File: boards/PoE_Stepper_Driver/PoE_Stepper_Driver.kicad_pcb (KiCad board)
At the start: 2 copper layers, 76 parts, among them J1 RJ45, J2 Motor, Q1 NMOS_POE, Q10 NMOS_POE, Q3 NMOS_POE, Q4 NMOS_POE, Q5 NMOS_POE, Q6 NMOS_POE, Q7 NMOS_POE, Q8 NMOS_POE, Q9 NMOS_POE, SW3 SW_Push, U1 LT4321, U14 DP83848C, U15 TMC429-I, U16 TMC2660C-PA, U2 LT4293, U3 STM32F407VETx, U4 NCP1117, U5 E48SC12010, X1 SXO53C, Y1 8MHz

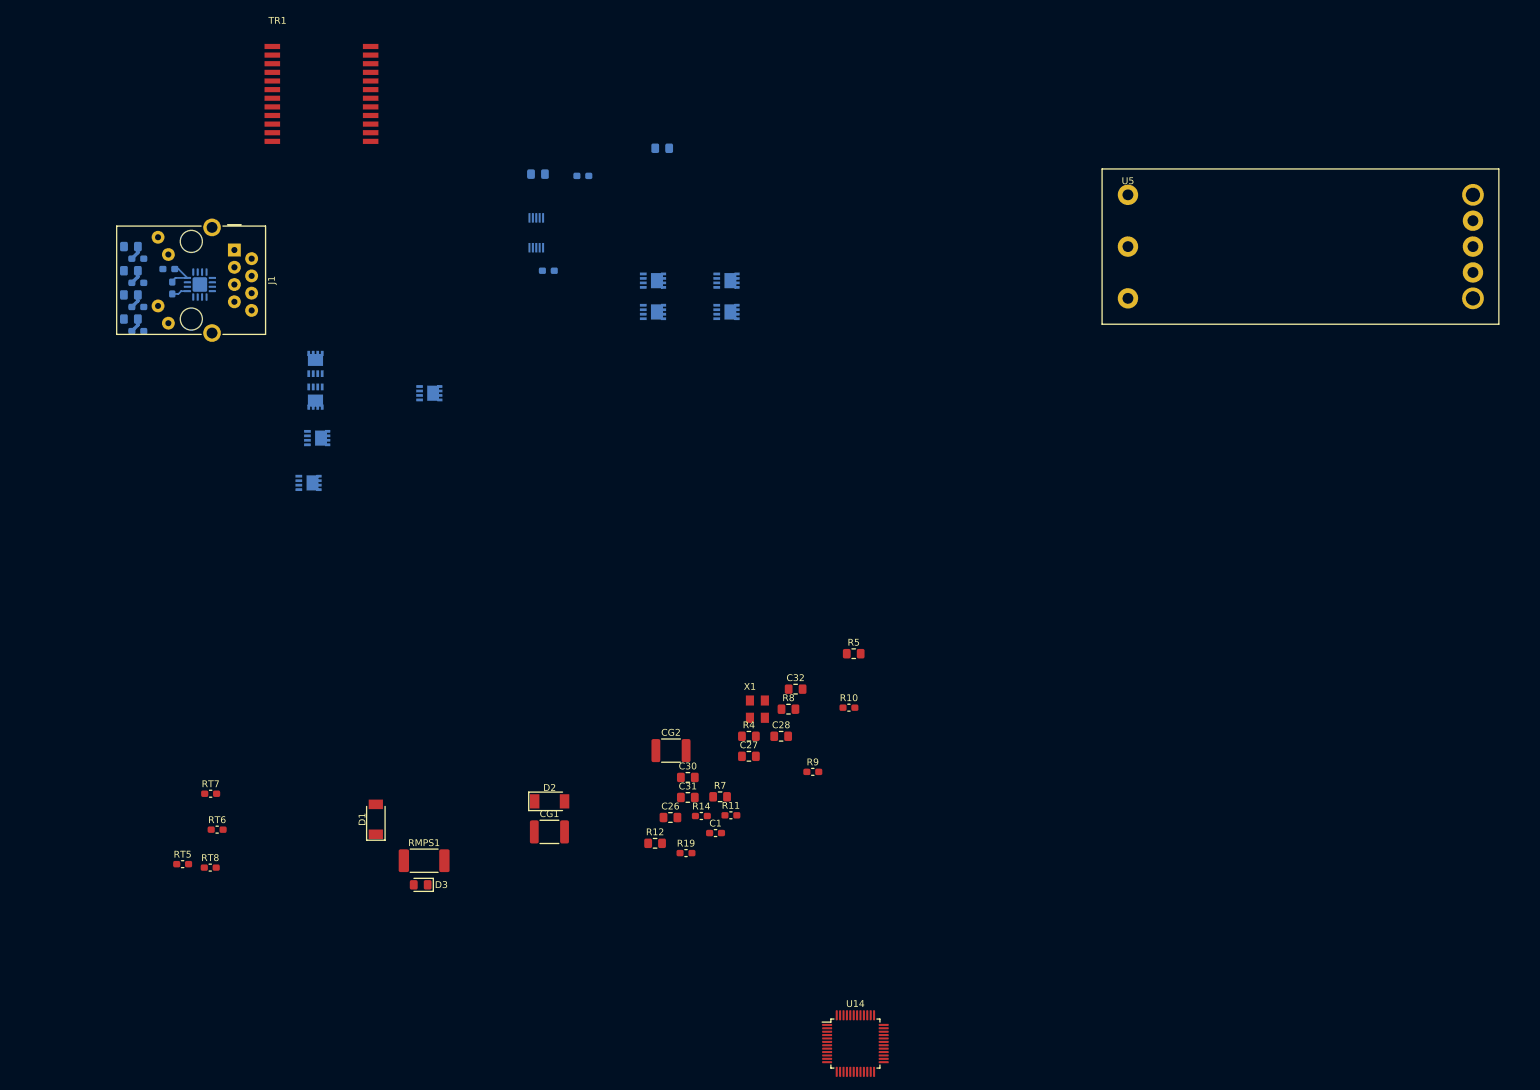
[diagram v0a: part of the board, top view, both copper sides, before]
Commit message: why tf is gnd connected to vout- bruhh
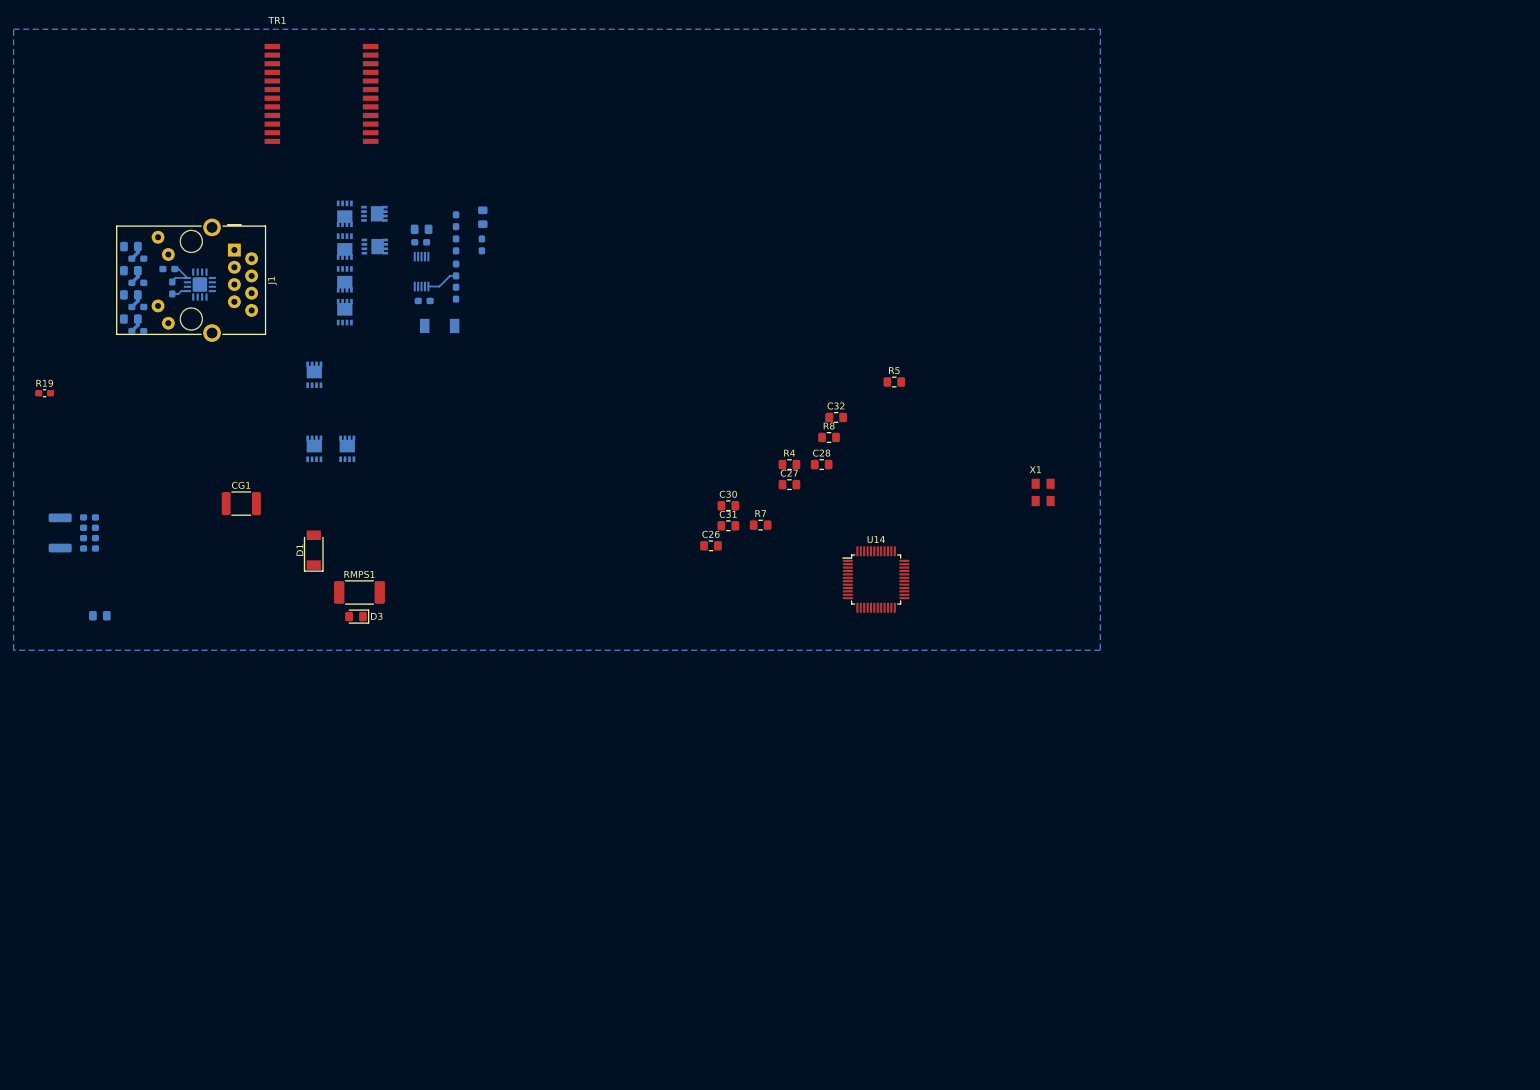
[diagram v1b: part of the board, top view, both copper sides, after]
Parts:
- removed U5: E48SC12010, PoE_Stepper_Driver:E48SC12010
- C1, CG2, D2, R10, R11, R12, R14, R9, RT5, RT6, RT7, RT8: moved to B.Cu
- Q1, Q10, Q3, Q4, Q5, Q6, Q7, Q8, Q9: footprint Package_SO:Vishay_PowerPAK_1212-8_Single -> Package_TO_SOT_SMD:LFPAK33
- moved R19 116.2 mm to (-5.59, 43.4)
- moved R6 107.7 mm to (2.54, 76.2)
- moved R12 95.6 mm to (58.9, 17.5), turned to 90 degrees
- moved CG2 95.5 mm to (-3.30, 64.0), turned to 270 degrees
- moved C1 94.7 mm to (55.0, 21.6), turned to 270 degrees
- moved R14 90.1 mm to (58.8, 21.6), turned to 270 degrees
- moved R11 89.9 mm to (55.0, 25.3), turned to 90 degrees
- moved R9 87.9 mm to (55.0, 28.7), turned to 90 degrees
- moved R10 86.6 mm to (50.3, 29.8), turned to 180 degrees
- moved D2 71.8 mm to (52.6, 33.5), turned to 180 degrees
- moved U14 68.4 mm to (116.8, 70.9)
- moved CG1 66.3 mm to (23.4, 59.7)
- moved Q9 62.3 mm to (34.1, 40.7), turned to 90 degrees
- moved Q3 55.7 mm to (34.1, 51.6), turned to 90 degrees
- moved RT8 54.5 mm to (1.02, 61.7), turned to 180 degrees
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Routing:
- net Net-(R11-Pad1): track 0.00 -> 4.73 mm
- added copper zone on B.Cu, net VOUT-

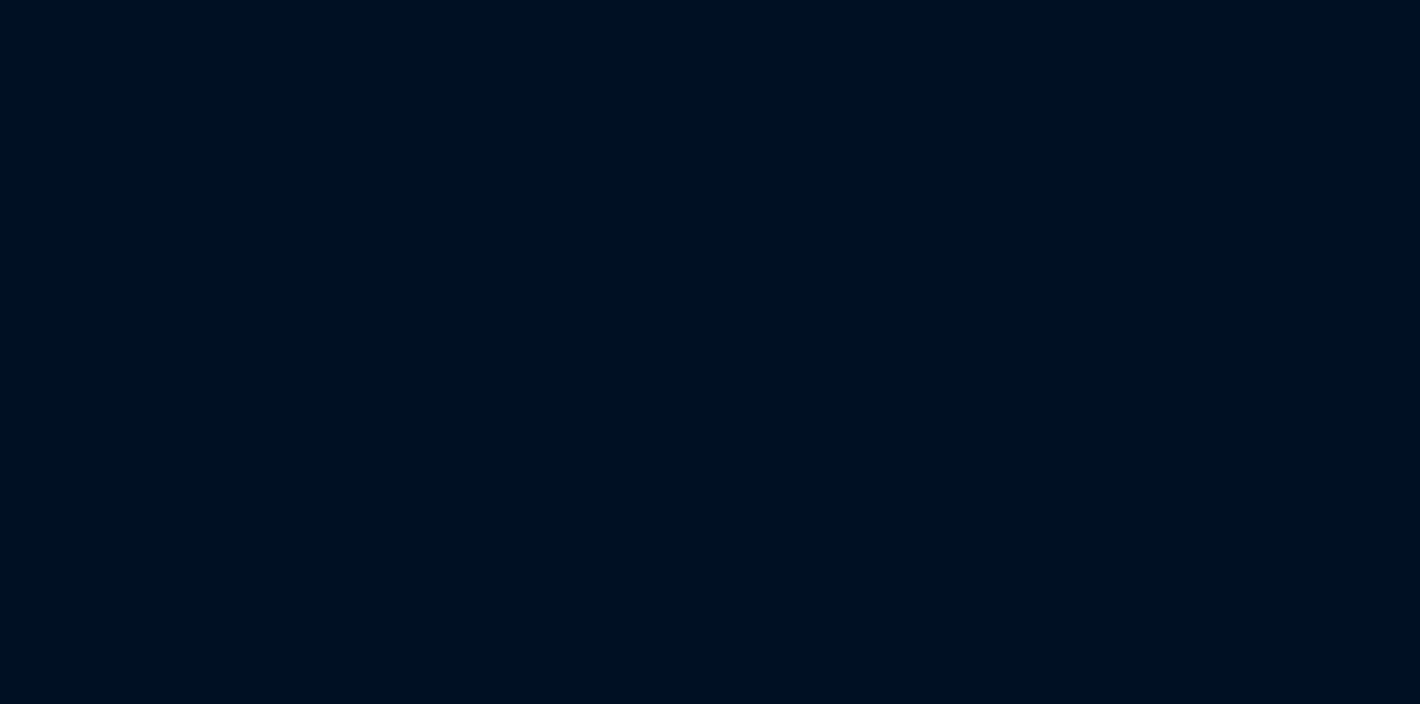
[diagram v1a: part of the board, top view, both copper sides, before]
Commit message: fixed ground issue
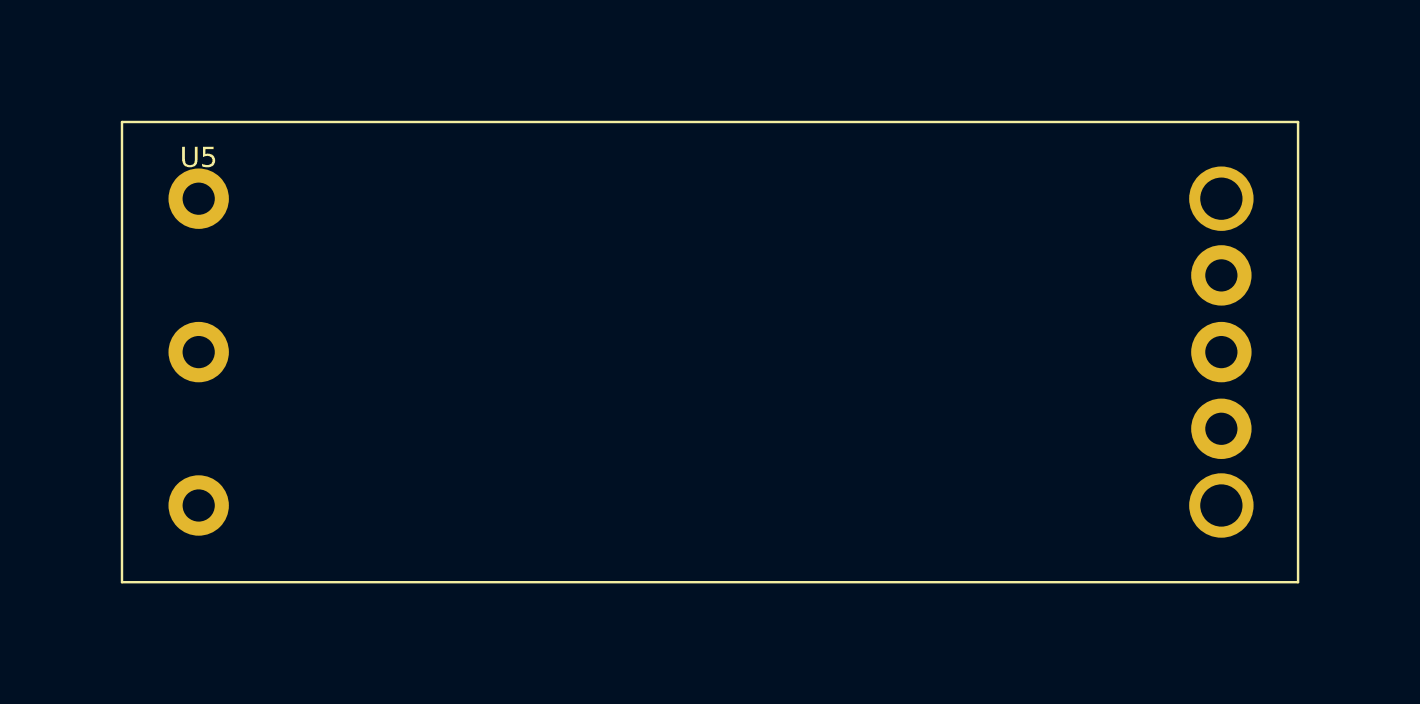
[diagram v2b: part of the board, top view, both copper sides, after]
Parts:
- added U5: E48SC12010, PoE_Stepper_Driver:E48SC12010, F.Cu at (73.9, 0.76)
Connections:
- C10 pad 2: VOUT- -> GND
- C14 pad 2: VOUT- -> GND
- C17 pad 2: VOUT- -> GND
- C26 pad 2: VOUT- -> GND
- C27 pad 2: VOUT- -> GND
- C28 pad 2: VOUT- -> GND
- C30 pad 2: VOUT- -> GND
- C31 pad 2: VOUT- -> GND
- C32 pad 2: VOUT- -> GND
- C34 pad 2: VOUT- -> GND
- C35 pad 2: VOUT- -> GND
- C36 pad 2: VOUT- -> GND
- C37 pad 2: VOUT- -> GND
- C38 pad 2: VOUT- -> GND
- C39 pad 2: VOUT- -> GND
- C7 pad 2: VOUT- -> GND
- R19 pad 2: VOUT- -> GND
- SW3 pad 2: VOUT- -> GND
- TR1 pad 2: VOUT- -> GND
- TR1 pad 3: VOUT- -> GND
- U14 pad 15: VOUT- -> GND
- U14 pad 19: VOUT- -> GND
- U14 pad 35: VOUT- -> GND
- U14 pad 36: VOUT- -> GND
- U14 pad 47: VOUT- -> GND
- U15 pad 15: VOUT- -> GND
- U15 pad 4: VOUT- -> GND
- U16 pad 17: VOUT- -> GND
- U16 pad 19: VOUT- -> GND
- U16 pad 39: VOUT- -> GND
- U16 pad 43: VOUT- -> GND
- U16 pad 44: VOUT- -> GND
- U3 pad 10: VOUT- -> GND
- U3 pad 20: VOUT- -> GND
- U3 pad 27: VOUT- -> GND
- U3 pad 74: VOUT- -> GND
- U3 pad 99: VOUT- -> GND
- U4 pad 1: VOUT- -> GND
- X1 pad 2: VOUT- -> GND

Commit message: finished footprint assignment
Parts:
- added C11: 0.1uF, Capacitor_SMD:C_0805_2012Metric_Pad1.15x1.40mm_HandSolder, F.Cu at (291.1, 35.4)
- added C12: 20pF, Capacitor_SMD:C_0603_1608Metric_Pad1.05x0.95mm_HandSolder, F.Cu at (253.6, 46.6)
- added C13: 0.1uF, Capacitor_SMD:C_0805_2012Metric_Pad1.15x1.40mm_HandSolder, F.Cu at (290.3, 26.5)
- added C15: 10nF, Capacitor_SMD:C_0805_2012Metric_Pad1.15x1.40mm_HandSolder, F.Cu at (246.2, 33.1)
- added C16: 10nF, Capacitor_SMD:C_0805_2012Metric_Pad1.15x1.40mm_HandSolder, F.Cu at (234.6, 40.6)
- added C18: 220nF, Capacitor_SMD:C_0805_2012Metric_Pad1.15x1.40mm_HandSolder, F.Cu at (250.4, 27.8)
- added C19: 100uF, Capacitor_THT:CP_Radial_D8.0mm_P3.50mm, F.Cu at (229.5, 33.4)
- added C20: 10uF, Capacitor_SMD:C_1206_3216Metric_Pad1.42x1.75mm_HandSolder, F.Cu at (229.3, 39.9)
- added C21: 100uF, Capacitor_THT:CP_Radial_D8.0mm_P3.50mm, F.Cu at (241.5, 26.9)
- added C22: 10uF, Capacitor_SMD:C_1206_3216Metric_Pad1.42x1.75mm_HandSolder, F.Cu at (239.0, 37.5)
- added C23: 470nF, Capacitor_SMD:C_0805_2012Metric_Pad1.15x1.40mm_HandSolder, F.Cu at (258.1, 23.6)
- added C24: 0.1uF, Capacitor_SMD:C_0805_2012Metric_Pad1.15x1.40mm_HandSolder, F.Cu at (285.6, 23.6)
- added C25: 0.1uF, Capacitor_SMD:C_0805_2012Metric_Pad1.15x1.40mm_HandSolder, F.Cu at (276.9, 38.0)
- added C29: 10uF, Capacitor_SMD:C_0805_2012Metric_Pad1.15x1.40mm_HandSolder, F.Cu at (290.3, 23.6)
- added C33: 10nF, Capacitor_SMD:C_0805_2012Metric_Pad1.15x1.40mm_HandSolder, F.Cu at (285.6, 29.5)
- added C4: 22uF, Capacitor_SMD:CP_Elec_8x10.5, F.Cu at (271.9, 27.1)
- added C40: 47uF, Capacitor_THT:CP_Radial_D8.0mm_P3.50mm, F.Cu at (240.2, 50.1)
- added C6: 20pF, Capacitor_SMD:C_0603_1608Metric_Pad1.05x0.95mm_HandSolder, F.Cu at (243.9, 56.1)
- added C8: 10uF, Capacitor_SMD:CP_Elec_6.3x5.4, F.Cu at (231.6, 57.5)
- added C9: 10uF, Capacitor_SMD:CP_Elec_6.3x5.4, F.Cu at (231.6, 49.4)
- added J3: Limits, Connector_JST:JST_PH_B4B-PH-K_1x04_P2.00mm_Vertical, F.Cu at (229.3, 24.8)
- added JP1: Jumper_NO_Small, Connector_PinHeader_2.54mm:PinHeader_1x02_P2.54mm_Vertical, F.Cu at (272.2, 34.5)
- added JP2: Jumper_NO_Small, Connector_PinHeader_2.54mm:PinHeader_1x02_P2.54mm_Vertical, F.Cu at (280.9, 31.6)
- added JP3: Jumper_NO_Small, Connector_PinHeader_2.54mm:PinHeader_1x02_P2.54mm_Vertical, F.Cu at (280.9, 24.4)
- added JP4: Jumper_NO_Small, Connector_PinHeader_2.54mm:PinHeader_1x02_P2.54mm_Vertical, F.Cu at (267.5, 34.5)
- added R1: 470, Resistor_SMD:R_0805_2012Metric_Pad1.15x1.40mm_HandSolder, F.Cu at (239.3, 59.3)
- added R2: 470, Resistor_SMD:R_0805_2012Metric_Pad1.15x1.40mm_HandSolder, F.Cu at (249.1, 46.8)
- added R20: 150, Resistor_SMD:R_0805_2012Metric_Pad1.15x1.40mm_HandSolder, F.Cu at (286.4, 38.3)
- added R21: 18, Resistor_SMD:R_0805_2012Metric_Pad1.15x1.40mm_HandSolder, F.Cu at (295.1, 29.5)
- added R22: 18, Resistor_SMD:R_0805_2012Metric_Pad1.15x1.40mm_HandSolder, F.Cu at (290.3, 32.4)
- added R23: 10k, Resistor_SMD:R_0805_2012Metric_Pad1.15x1.40mm_HandSolder, F.Cu at (250.9, 33.7)
- added R24: 10k, Resistor_SMD:R_0805_2012Metric_Pad1.15x1.40mm_HandSolder, F.Cu at (255.1, 27.8)
- added R25: 10k, Resistor_SMD:R_0805_2012Metric_Pad1.15x1.40mm_HandSolder, F.Cu at (250.9, 30.7)
- added R26: 75m, Resistor_SMD:R_2010_5025Metric_Pad1.52x2.65mm_HandSolder, F.Cu at (251.9, 24.2)
- added R27: 22, Resistor_SMD:R_0805_2012Metric_Pad1.15x1.40mm_HandSolder, F.Cu at (244.4, 37.3)
- added R28: 75m, Resistor_SMD:R_2010_5025Metric_Pad1.52x2.65mm_HandSolder, F.Cu at (239.9, 33.8)
- added R29: 22, Resistor_SMD:R_0805_2012Metric_Pad1.15x1.40mm_HandSolder, F.Cu at (239.4, 40.6)
- added R3: 220, Resistor_SMD:R_0603_1608Metric_Pad1.05x0.95mm_HandSolder, F.Cu at (248.9, 49.5)
- added R30: 2.2k, Resistor_SMD:R_0805_2012Metric_Pad1.15x1.40mm_HandSolder, F.Cu at (285.6, 26.5)
- added R31: 2.2k, Resistor_SMD:R_0805_2012Metric_Pad1.15x1.40mm_HandSolder, F.Cu at (286.4, 35.4)
- added R32: 4.7k, Resistor_SMD:R_0805_2012Metric_Pad1.15x1.40mm_HandSolder, F.Cu at (295.1, 26.5)
- added R33: 18, Resistor_SMD:R_0805_2012Metric_Pad1.15x1.40mm_HandSolder, F.Cu at (290.3, 29.5)
- added R34: 18, Resistor_SMD:R_0805_2012Metric_Pad1.15x1.40mm_HandSolder, F.Cu at (295.1, 23.6)
- added R35: 2.2k, Resistor_SMD:R_0805_2012Metric_Pad1.15x1.40mm_HandSolder, F.Cu at (285.6, 32.4)
- added R36: 2.2k, Resistor_SMD:R_0805_2012Metric_Pad1.15x1.40mm_HandSolder, F.Cu at (281.6, 38.0)
- added R37: 10k, Resistor_SMD:R_0805_2012Metric_Pad1.15x1.40mm_HandSolder, F.Cu at (239.3, 56.3)
- R19: footprint Resistor_SMD:R_0603_1608Metric_Pad1.05x0.95mm_HandSolder -> Resistor_SMD:R_0805_2012Metric_Pad1.15x1.40mm_HandSolder
- moved Q1 34.6 mm to (42.9, 17.3), turned to 180 degrees
- moved Q3 23.6 mm to (37.3, 28.2), turned to 0 degrees
- moved Q9 8.35 mm to (37.3, 33.0), turned to 0 degrees
- moved D2 6.48 mm to (46.7, 36.3)
- moved C1 5.79 mm to (49.4, 23.1)
- moved C3 5.79 mm to (44.3, 20.8)
- moved Q5 5.79 mm to (37.4, 23.4)
- moved Q7 5.79 mm to (37.4, 18.5)
- moved R10 5.79 mm to (44.7, 31.4)
- moved R11 5.79 mm to (49.4, 26.8)
- moved R13 5.79 mm to (49.4, 19.6)
- moved R14 5.79 mm to (53.2, 23.1)
- moved R15 5.79 mm to (44.2, 22.7)
- moved R9 5.79 mm to (49.4, 30.2)
- moved U2 5.79 mm to (44.3, 27.1)
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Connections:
- U5 pad 1: Net-(C41-Pad1) -> VOUT+
- U5 pad 3: Net-(C42-Pad2) -> VOUT-

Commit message: almost finished ethernet layout
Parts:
- added C2: 0.1uF, Capacitor_SMD:C_0805_2012Metric_Pad1.15x1.40mm_HandSolder, F.Cu at (93.5, 25.1)
- R4, R5: moved to B.Cu
- moved U4 267.2 mm to (72.1, 56.4)
- moved JP2 218.3 mm to (62.7, 40.4), turned to 90 degrees
- moved R19 212.9 mm to (199.6, -13.2), turned to 90 degrees
- moved JP4 204.8 mm to (62.7, 37.8), turned to 90 degrees
- moved JP3 204.6 mm to (76.7, 37.8), turned to 270 degrees
- moved JP1 195.6 mm to (76.7, 40.4), turned to 270 degrees
- moved U3 173.3 mm to (137.2, 8.89)
- moved CG2 79.3 mm to (62.5, 19.8)
- moved R6 76.8 mm to (69.1, 37.8)
- moved RT5 72.4 mm to (58.4, 22.1), turned to 0 degrees
- moved RT6 72.4 mm to (58.4, 20.6), turned to 0 degrees
- moved RT7 72.4 mm to (58.4, 19.1), turned to 0 degrees
- moved RT8 72.4 mm to (58.4, 17.5), turned to 0 degrees
- moved D3 39.0 mm to (52.2, 39.2), turned to 270 degrees
- moved R5 37.9 mm to (81.8, 37.8)
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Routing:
- net PWRGD: track 0.00 -> 60.4 mm, vias 0 -> 2
- net /Ethernet/TG45: track 0.00 -> 49.0 mm, vias 0 -> 2
- net /Ethernet/VPORTP: track 4.96 -> 53.0 mm, vias 0 -> 2
- net /Ethernet/POE_CT12: track 0.00 -> 41.5 mm, vias 0 -> 1
- net /Ethernet/BG45: track 0.00 -> 40.0 mm, vias 0 -> 2
- net /Ethernet/POE_CT78: track 0.00 -> 32.9 mm, vias 0 -> 3
- net /Ethernet/TG36: track 0.00 -> 32.7 mm, vias 0 -> 4
- net /Ethernet/POE_CT45: track 0.00 -> 32.3 mm, vias 0 -> 3
- net /Ethernet/BG36: track 0.00 -> 30.4 mm, vias 0 -> 2
- net /Ethernet/POE_CT36: track 0.00 -> 26.1 mm, vias 0 -> 3
- net /Ethernet/TG12: track 0.00 -> 23.0 mm, vias 0 -> 2
- net /Ethernet/BG12: track 0.00 -> 20.8 mm, vias 0 -> 2
- net /Ethernet/TG78: track 0.00 -> 20.2 mm
- net Net-(RT5-Pad1): track 0.00 -> 18.9 mm, vias 0 -> 1
- net Net-(J1-Pad5): track 0.00 -> 18.6 mm, vias 0 -> 1
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- added copper zone on B.Cu, net /Ethernet/POE_CT12
- added copper zone on B.Cu, net /Ethernet/POE_CT36
- added copper zone on B.Cu, net /Ethernet/POE_CT45
- added copper zone on B.Cu, net /Ethernet/POE_CT78
- added copper zone on B.Cu, net /Ethernet/VPORTP
- added copper zone on B.Cu, net Net-(CG1-Pad1)
- added copper zone on B.Cu, net Net-(CG2-Pad1)
- added copper zone on F.Cu, net VOUT+
- added copper zone on F.Cu, net VOUT-
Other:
- board outline added: 99.1 x 71.1 mm
